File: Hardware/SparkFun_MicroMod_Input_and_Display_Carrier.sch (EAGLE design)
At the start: 69 parts, among them J1 MICROMOD-2222-C, J2 MICRO-SD, J3 USB-C_Prog, J4 AVR_SPI_PROG_3X2TESTPOINTS, J5 2.4" TFT, J6 QWIIC_RA, J7 CORTEX_JTAG_DEBUG, Q1 1.1A/600mΩ, Q2 600mA/40V, U2 ATTINY84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

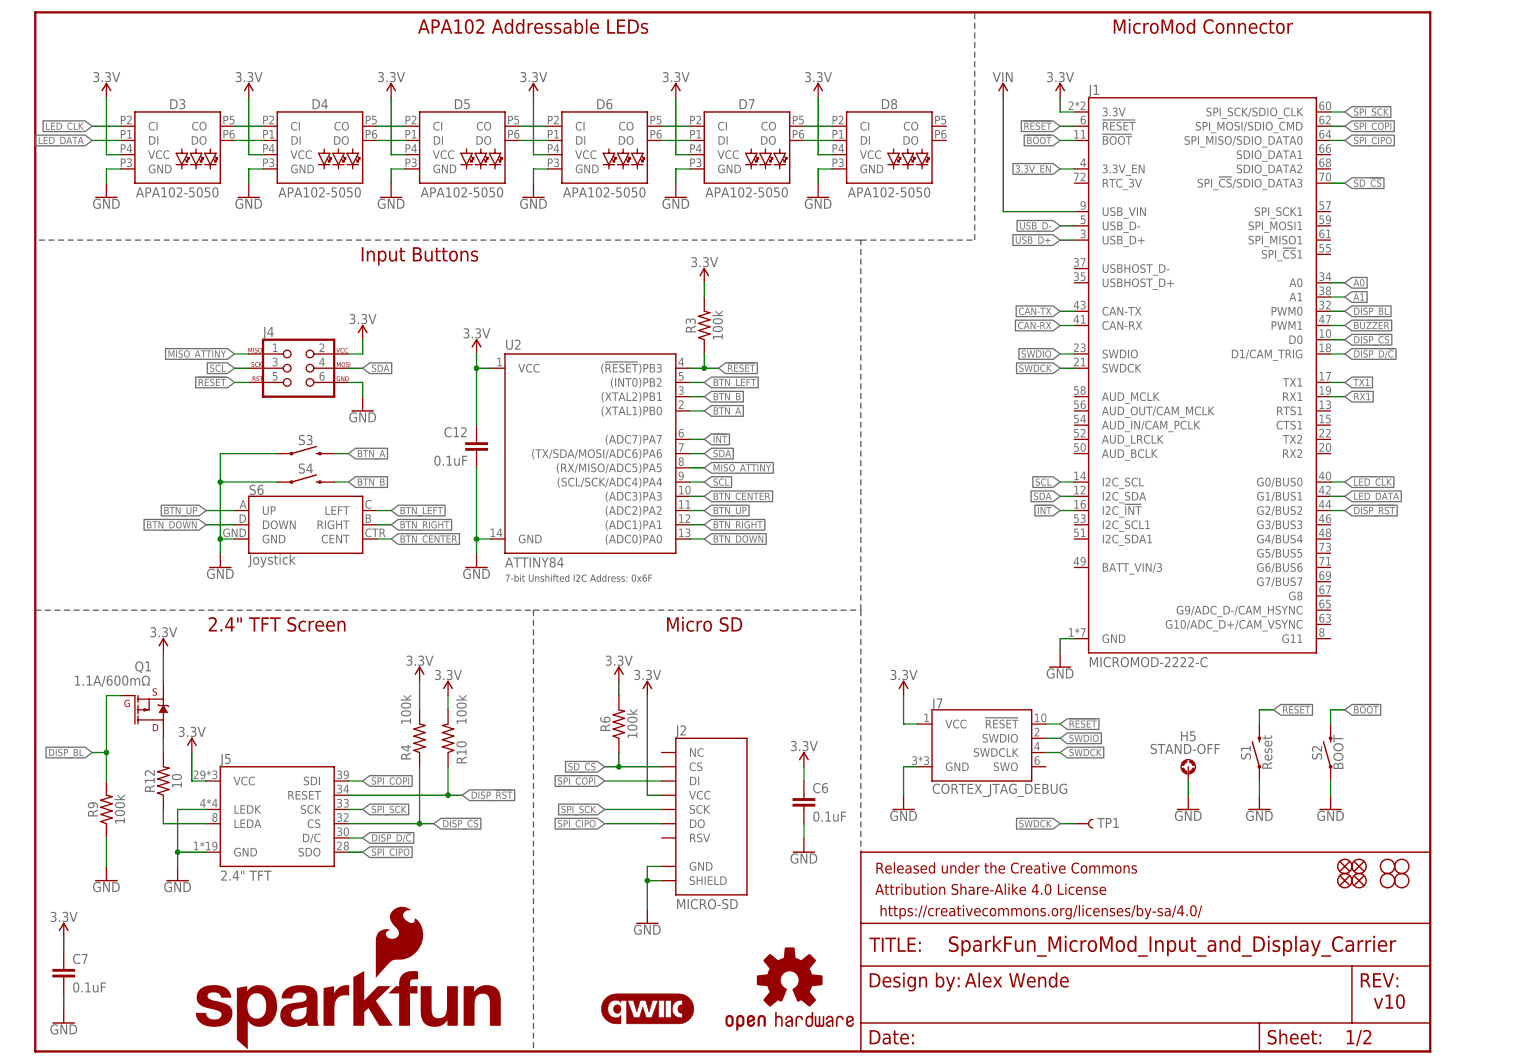
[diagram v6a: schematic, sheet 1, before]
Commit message: v10 cleanup
-Updated active low labels
-Fixed Attiny I2C address
-Updated measures layer
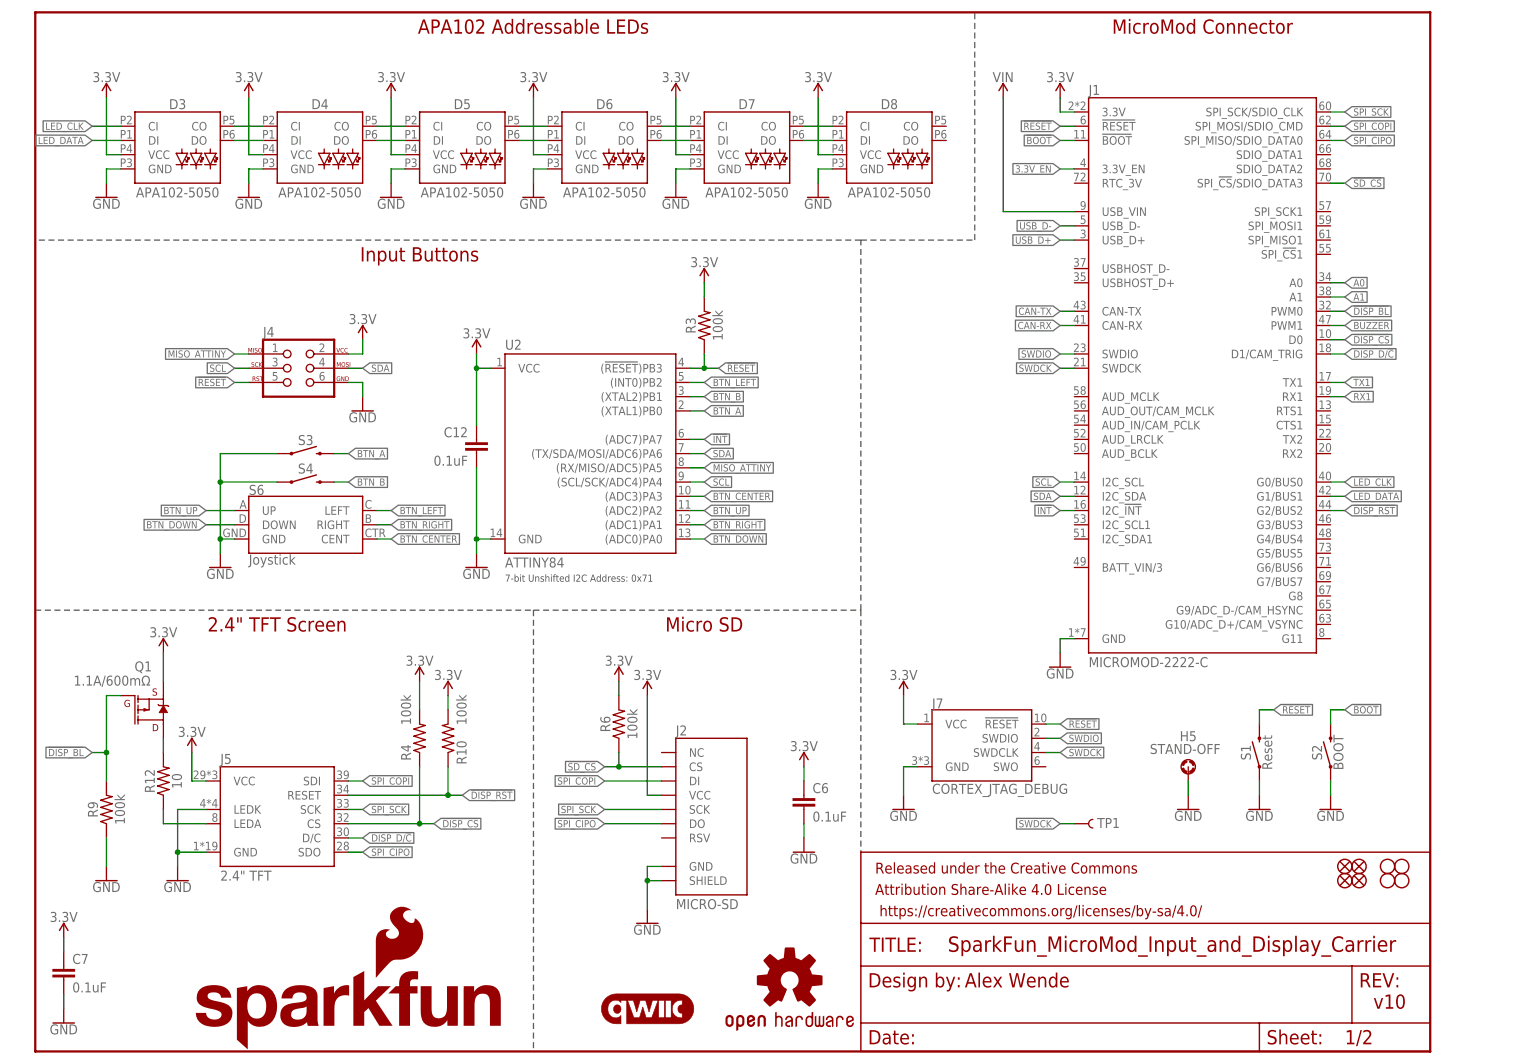
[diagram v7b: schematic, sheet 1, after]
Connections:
- net DISP_!CS renamed !DISP_CS
- net DISP_!RST renamed !DISP_RST
- net DISP_BL renamed !DISP_BL
- net SD_!CS renamed !SD_CS
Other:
- note added: "7-bit Unshifted I2C Address: 0x71"
- note removed: "7-bit Unshifted I2C Address: 0x6F"
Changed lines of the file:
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@@
 <sheet>
 <plain>
-<text x="83.82" y="83.82" size="1.27" layer="97" font="vector">7-bit Unshifted I2C Address: 0x6F</text>
+<text x="83.82" y="83.82" size="1.27" layer="97" font="vector">7-bit Unshifted I2C Address: 0x71</text>
 <text x="165.862" y="11.43" size="2.54" layer="94" font="vector">Alex Wende</text>
 <text x="238.76" y="7.62" size="2.54" layer="94" font="vector">v10</text>
@@
 </segment>
 </net>
-<net name="SD_!CS" class="0">
+<net name="!SD_CS" class="0">
 <segment>
 <pinref part="J1" gate="J1" pin="SPI_!CS!/SDIO_DATA3"/>
@@
 </segment>
 </net>
-<net name="DISP_!CS" class="0">
+<net name="!DISP_CS" class="0">
 <segment>
 <pinref part="J1" gate="J1" pin="D0"/>
@@
 </segment>
 </net>
-<net name="DISP_BL" class="0">
+<net name="!DISP_BL" class="0">
 <segment>
 <pinref part="J1" gate="J1" pin="PWM0"/>
@@
 </segment>
 </net>
-<net name="DISP_!RST" class="0">
+<net name="!DISP_RST" class="0">
 <segment>
 <pinref part="J5" gate="G$1" pin="RESET"/>

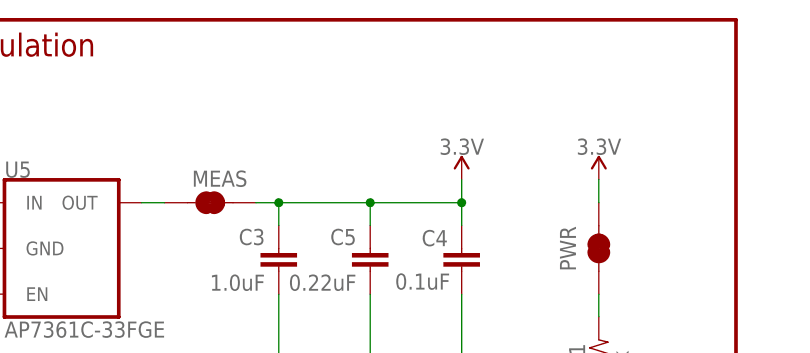
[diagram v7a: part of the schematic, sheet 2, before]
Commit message: QC fixes
- Added note for MEAS jumper
- Adjusted button B label
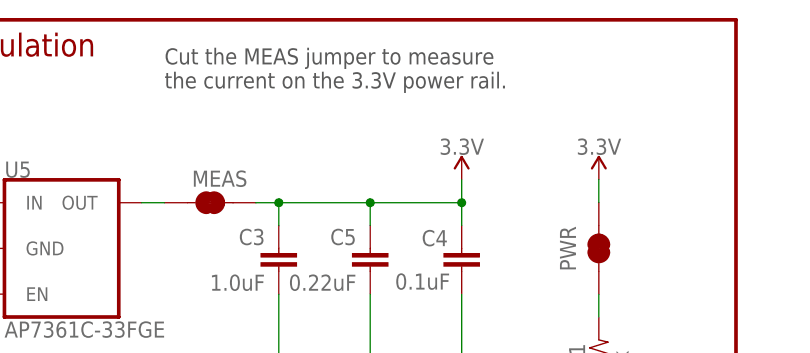
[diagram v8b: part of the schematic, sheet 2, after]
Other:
- note added: "Cut the MEAS jumper to measure the current on the 3.3V power rail."
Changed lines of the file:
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@@
 <text x="218.44" y="111.76" size="2.54" layer="94" font="vector" align="center">IO Connector</text>
 <text x="162.56" y="177.8" size="1.778" layer="97" font="vector" align="center">6V Max</text>
+<text x="185.42" y="177.8" size="1.778" layer="97">Cut the MEAS jumper to measure
+the current on the 3.3V power rail.</text>
 </plain>
 <instances>
